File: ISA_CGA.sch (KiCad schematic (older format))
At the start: 29 parts, among them U1 74S112, U11 74LS74, U12 74LS393, U13 74LS08, U14 74LS32, U15 74LS00, U16 74LS04, U2 74LS74, U20 74LS04, U22 74LS51, U23 74LS32, U25 74LS00, U26 74LS04, U27 74LS51, U28 74LS10, U29 74S04, U3 74S86, U30 74LS32, U31 74S08, U41 74LS08, U42 74LS86, U46 74LS00, U47 74LS51, U48 74LS51, U49 74LS02, U6 74LS04, U62 74LS125, U65 74LS02, U68 74LS86

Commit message: More sheet 5
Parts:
- added U44: 74S74, Package_DIP:DIP-14_W7.62mm_LongPads, symbol 74xx:74LS74
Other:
- moved on the sheet: U29G, U30E, U31E, U41E, U42E
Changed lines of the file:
@@
 L 74xx:74LS08 U?
 U 5 1 61D13A76
-P 4150 5150
+P 3550 5150
 AR Path="/60463C10/61D13A76" Ref="U?"  Part="3"
 AR Path="/61D13A76" Ref="U31"  Part="5"
-F 0 "U31" H 4000 5500 50  0000 C CNN
-F 1 "74S08" H 4300 5500 50  0000 C CNN
-F 2 "Package_DIP:DIP-14_W7.62mm_LongPads" H 4150 5150 50  0001 C CNN
-F 3 "http://www.ti.com/lit/gpn/sn74LS08" H 4150 5150 50  0001 C CNN
-	5    4150 5150
+F 0 "U31" H 3400 5500 50  0000 C CNN
+F 1 "74S08" H 3700 5500 50  0000 C CNN
+F 2 "Package_DIP:DIP-14_W7.62mm_LongPads" H 3550 5150 50  0001 C CNN
+F 3 "http://www.ti.com/lit/gpn/sn74LS08" H 3550 5150 50  0001 C CNN
+	5    3550 5150
 	1    0    0    -1
 $EndComp
@@
 L 74xx:74LS86 U?
 U 5 1 629C2DFD
-P 5350 5150
+P 4750 5150
 AR Path="/60463C10/629C2DFD" Ref="U?"  Part="4"
 AR Path="/60463C57/629C2DFD" Ref="U?"  Part="1"
 AR Path="/629C2DFD" Ref="U42"  Part="5"
-F 0 "U42" H 5500 5500 50  0000 C CNN
-F 1 "74LS86" H 5200 5500 50  0000 C CNN
-F 2 "Package_DIP:DIP-14_W7.62mm_LongPads" H 5350 5150 50  0001 C CNN
-F 3 "74xx/74ls86.pdf" H 5350 5150 50  0001 C CNN
-	5    5350 5150
+F 0 "U42" H 4900 5500 50  0000 C CNN
+F 1 "74LS86" H 4600 5500 50  0000 C CNN
+F 2 "Package_DIP:DIP-14_W7.62mm_LongPads" H 4750 5150 50  0001 C CNN
+F 3 "74xx/74ls86.pdf" H 4750 5150 50  0001 C CNN
+	5    4750 5150
 	-1   0    0    -1
 $EndComp
@@
 L 74xx:74LS32 U?
 U 5 1 62AC6F3C
-P 3550 5150
+P 2950 5150
 AR Path="/60463C57/62AC6F3C" Ref="U?"  Part="3"
 AR Path="/62AC6F3C" Ref="U30"  Part="5"
-F 0 "U30" H 3400 5500 50  0000 C CNN
-F 1 "74LS32" H 3700 5500 50  0000 C CNN
-F 2 "" H 3550 5150 50  0001 C CNN
-F 3 "http://www.ti.com/lit/gpn/sn74LS32" H 3550 5150 50  0001 C CNN
-	5    3550 5150
+F 0 "U30" H 2800 5500 50  0000 C CNN
+F 1 "74LS32" H 3100 5500 50  0000 C CNN
+F 2 "" H 2950 5150 50  0001 C CNN
+F 3 "http://www.ti.com/lit/gpn/sn74LS32" H 2950 5150 50  0001 C CNN
+	5    2950 5150
 	1    0    0    -1
 $EndComp
@@
 L 74xx:74LS08 U?
 U 5 1 62CA5B30
-P 4750 5150
+P 4150 5150
 AR Path="/60463C57/62CA5B30" Ref="U?"  Part="4"
 AR Path="/62CA5B30" Ref="U41"  Part="5"
-F 0 "U41" H 4600 5500 50  0000 C CNN
-F 1 "74LS08" H 4900 5500 50  0000 C CNN
-F 2 "Package_DIP:DIP-14_W7.62mm_LongPads" H 4750 5150 50  0001 C CNN
-F 3 "http://www.ti.com/lit/gpn/sn74LS08" H 4750 5150 50  0001 C CNN
-	5    4750 5150
+F 0 "U41" H 4000 5500 50  0000 C CNN
+F 1 "74LS08" H 4300 5500 50  0000 C CNN
+F 2 "Package_DIP:DIP-14_W7.62mm_LongPads" H 4150 5150 50  0001 C CNN
+F 3 "http://www.ti.com/lit/gpn/sn74LS08" H 4150 5150 50  0001 C CNN
+	5    4150 5150
 	1    0    0    -1
 $EndComp
@@
 L 74xx:74LS04 U?
 U 7 1 63CE58E6
-P 2950 5150
+P 2350 5150
 AR Path="/60463C57/63CE58E6" Ref="U?"  Part="6"
 AR Path="/60463CC5/63CE58E6" Ref="U?"  Part="4"
 AR Path="/63CE58E6" Ref="U29"  Part="7"
-F 0 "U29" H 2800 5500 50  0000 C CNN
-F 1 "74S04" H 3100 5500 50  0000 C CNN
-F 2 "Package_DIP:DIP-14_W7.62mm_LongPads" H 2950 5150 50  0001 C CNN
-F 3 "http://www.ti.com/lit/gpn/sn74LS04" H 2950 5150 50  0001 C CNN
-	7    2950 5150
+F 0 "U29" H 2200 5500 50  0000 C CNN
+F 1 "74S04" H 2500 5500 50  0000 C CNN
+F 2 "Package_DIP:DIP-14_W7.62mm_LongPads" H 2350 5150 50  0001 C CNN
+F 3 "http://www.ti.com/lit/gpn/sn74LS04" H 2350 5150 50  0001 C CNN
+	7    2350 5150
 	1    0    0    -1
 $EndComp
@@
 	1    0    0    -1
 $EndComp
+$Comp
+L 74xx:74LS74 U?
+U 3 1 64BD6305
+P 5350 5150
+AR Path="/60463CF3/64BD6305" Ref="U?"  Part="1"
+AR Path="/64BD6305" Ref="U44"  Part="3"
+F 0 "U44" H 5200 5500 50  0000 C CNN
+F 1 "74S74" H 5500 5500 50  0000 C CNN
+F 2 "Package_DIP:DIP-14_W7.62mm_LongPads" H 5350 5150 50  0001 C CNN
+F 3 "74xx/74hc_hct74.pdf" H 5350 5150 50  0001 C CNN
+	3    5350 5150
+	1    0    0    -1
+$EndComp

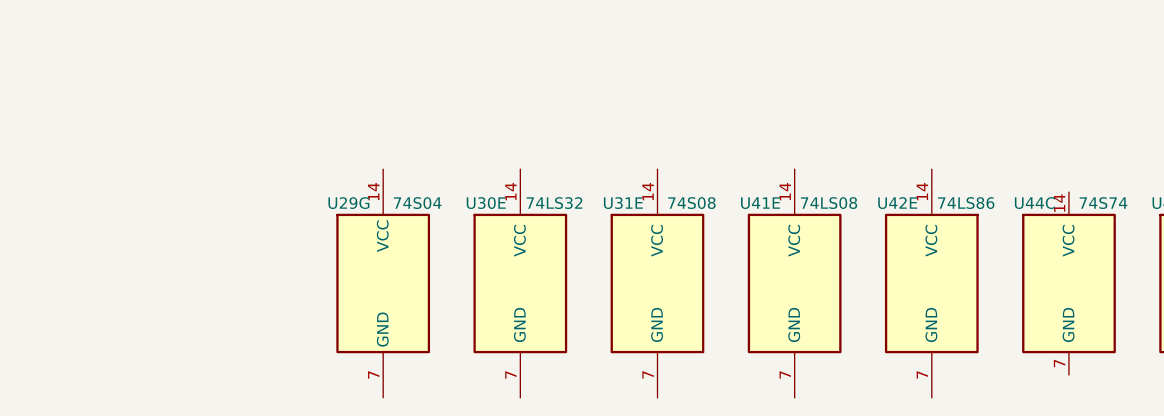
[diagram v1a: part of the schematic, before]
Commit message: More power connections for sheet 5
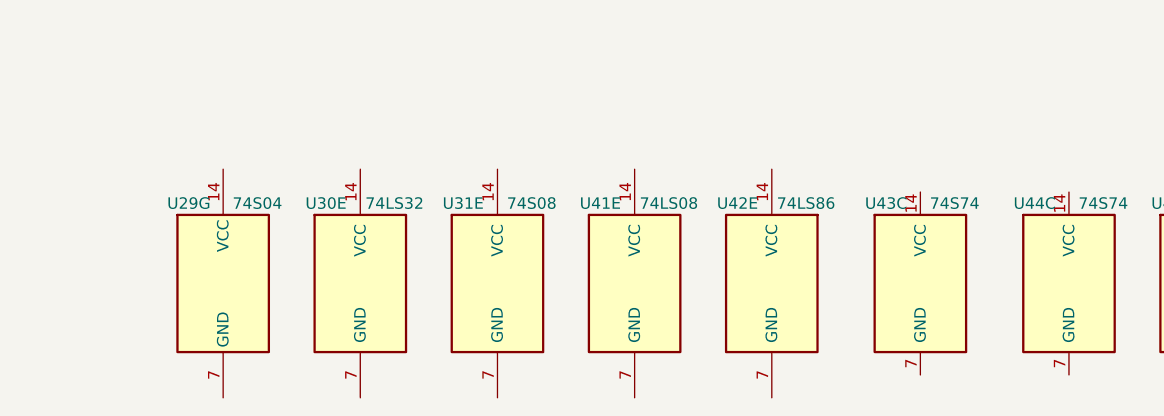
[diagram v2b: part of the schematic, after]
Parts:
- added U43: 74S74, Package_DIP:DIP-14_W7.62mm_LongPads, symbol 74xx:74LS74
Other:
- moved on the sheet: U29G, U30E, U31E, U41E, U42E
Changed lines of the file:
@@
 L 74xx:74LS08 U?
 U 5 1 61D13A76
-P 3550 5150
+P 2850 5150
 AR Path="/60463C10/61D13A76" Ref="U?"  Part="3"
 AR Path="/61D13A76" Ref="U31"  Part="5"
-F 0 "U31" H 3400 5500 50  0000 C CNN
-F 1 "74S08" H 3700 5500 50  0000 C CNN
-F 2 "Package_DIP:DIP-14_W7.62mm_LongPads" H 3550 5150 50  0001 C CNN
-F 3 "http://www.ti.com/lit/gpn/sn74LS08" H 3550 5150 50  0001 C CNN
-	5    3550 5150
+F 0 "U31" H 2700 5500 50  0000 C CNN
+F 1 "74S08" H 3000 5500 50  0000 C CNN
+F 2 "Package_DIP:DIP-14_W7.62mm_LongPads" H 2850 5150 50  0001 C CNN
+F 3 "http://www.ti.com/lit/gpn/sn74LS08" H 2850 5150 50  0001 C CNN
+	5    2850 5150
 	1    0    0    -1
 $EndComp
@@
 L 74xx:74LS86 U?
 U 5 1 629C2DFD
-P 4750 5150
+P 4050 5150
 AR Path="/60463C10/629C2DFD" Ref="U?"  Part="4"
 AR Path="/60463C57/629C2DFD" Ref="U?"  Part="1"
 AR Path="/629C2DFD" Ref="U42"  Part="5"
-F 0 "U42" H 4900 5500 50  0000 C CNN
-F 1 "74LS86" H 4600 5500 50  0000 C CNN
-F 2 "Package_DIP:DIP-14_W7.62mm_LongPads" H 4750 5150 50  0001 C CNN
-F 3 "74xx/74ls86.pdf" H 4750 5150 50  0001 C CNN
-	5    4750 5150
+F 0 "U42" H 4200 5500 50  0000 C CNN
+F 1 "74LS86" H 3900 5500 50  0000 C CNN
+F 2 "Package_DIP:DIP-14_W7.62mm_LongPads" H 4050 5150 50  0001 C CNN
+F 3 "74xx/74ls86.pdf" H 4050 5150 50  0001 C CNN
+	5    4050 5150
 	-1   0    0    -1
 $EndComp
@@
 L 74xx:74LS32 U?
 U 5 1 62AC6F3C
-P 2950 5150
+P 2250 5150
 AR Path="/60463C57/62AC6F3C" Ref="U?"  Part="3"
 AR Path="/62AC6F3C" Ref="U30"  Part="5"
-F 0 "U30" H 2800 5500 50  0000 C CNN
-F 1 "74LS32" H 3100 5500 50  0000 C CNN
-F 2 "" H 2950 5150 50  0001 C CNN
-F 3 "http://www.ti.com/lit/gpn/sn74LS32" H 2950 5150 50  0001 C CNN
-	5    2950 5150
+F 0 "U30" H 2100 5500 50  0000 C CNN
+F 1 "74LS32" H 2400 5500 50  0000 C CNN
+F 2 "" H 2250 5150 50  0001 C CNN
+F 3 "http://www.ti.com/lit/gpn/sn74LS32" H 2250 5150 50  0001 C CNN
+	5    2250 5150
 	1    0    0    -1
 $EndComp
@@
 L 74xx:74LS08 U?
 U 5 1 62CA5B30
-P 4150 5150
+P 3450 5150
 AR Path="/60463C57/62CA5B30" Ref="U?"  Part="4"
 AR Path="/62CA5B30" Ref="U41"  Part="5"
-F 0 "U41" H 4000 5500 50  0000 C CNN
-F 1 "74LS08" H 4300 5500 50  0000 C CNN
-F 2 "Package_DIP:DIP-14_W7.62mm_LongPads" H 4150 5150 50  0001 C CNN
-F 3 "http://www.ti.com/lit/gpn/sn74LS08" H 4150 5150 50  0001 C CNN
-	5    4150 5150
+F 0 "U41" H 3300 5500 50  0000 C CNN
+F 1 "74LS08" H 3600 5500 50  0000 C CNN
+F 2 "Package_DIP:DIP-14_W7.62mm_LongPads" H 3450 5150 50  0001 C CNN
+F 3 "http://www.ti.com/lit/gpn/sn74LS08" H 3450 5150 50  0001 C CNN
+	5    3450 5150
 	1    0    0    -1
 $EndComp
@@
 L 74xx:74LS04 U?
 U 7 1 63CE58E6
-P 2350 5150
+P 1650 5150
 AR Path="/60463C57/63CE58E6" Ref="U?"  Part="6"
 AR Path="/60463CC5/63CE58E6" Ref="U?"  Part="4"
 AR Path="/63CE58E6" Ref="U29"  Part="7"
-F 0 "U29" H 2200 5500 50  0000 C CNN
-F 1 "74S04" H 2500 5500 50  0000 C CNN
-F 2 "Package_DIP:DIP-14_W7.62mm_LongPads" H 2350 5150 50  0001 C CNN
-F 3 "http://www.ti.com/lit/gpn/sn74LS04" H 2350 5150 50  0001 C CNN
-	7    2350 5150
+F 0 "U29" H 1500 5500 50  0000 C CNN
+F 1 "74S04" H 1800 5500 50  0000 C CNN
+F 2 "Package_DIP:DIP-14_W7.62mm_LongPads" H 1650 5150 50  0001 C CNN
+F 3 "http://www.ti.com/lit/gpn/sn74LS04" H 1650 5150 50  0001 C CNN
+	7    1650 5150
 	1    0    0    -1
 $EndComp
@@
 	1    0    0    -1
 $EndComp
+$Comp
+L 74xx:74LS74 U?
+U 3 1 64C32517
+P 4700 5150
+AR Path="/60463CF3/64C32517" Ref="U?"  Part="1"
+AR Path="/64C32517" Ref="U43"  Part="3"
+F 0 "U43" H 4550 5500 50  0000 C CNN
+F 1 "74S74" H 4850 5500 50  0000 C CNN
+F 2 "Package_DIP:DIP-14_W7.62mm_LongPads" H 4700 5150 50  0001 C CNN
+F 3 "74xx/74hc_hct74.pdf" H 4700 5150 50  0001 C CNN
+	3    4700 5150
+	1    0    0    -1
+$EndComp

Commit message: Sheet 6
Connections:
- net VCC: now reaches U48.14 (VCC)
- net VCC: now also U1.16 (VCC), U11.14 (VCC), U12.14 (VCC), U13.14 (VCC), U14.14 (VCC), U15.14 (VCC), U16.14 (VCC), U2.14 (VCC), U20.14 (VCC), U22.14 (VCC), U23.14 (VCC), U25.14 (VCC), U26.14 (VCC), U27.14 (VCC), U28.14 (VCC), U29.14 (VCC), U3.14 (VCC), U30.14 (VCC), U31.14 (VCC), U41.14 (VCC), U42.14 (VCC), U46.14 (VCC), U47.14 (VCC), U49.14 (VCC), U6.14 (VCC), U62.14 (VCC), U65.14 (VCC), U68.14 (VCC)
- net GND: now reaches U48.7 (GND)
- net GND: now also U1.8 (GND), U11.7 (GND), U12.7 (GND), U13.7 (GND), U14.7 (GND), U15.7 (GND), U16.7 (GND), U2.7 (GND), U20.7 (GND), U22.7 (GND), U23.7 (GND), U25.7 (GND), U26.7 (GND), U27.7 (GND), U28.7 (GND), U29.7 (GND), U3.7 (GND), U30.7 (GND), U31.7 (GND), U41.7 (GND), U42.7 (GND), U46.7 (GND), U47.7 (GND), U49.7 (GND), U6.7 (GND), U62.7 (GND), U65.7 (GND), U68.7 (GND)
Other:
- moved on the sheet: U29G, U30E, U31E, U41E, U42E, U43C, U44C, U46E, U47C, U48C, U49E, U62E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

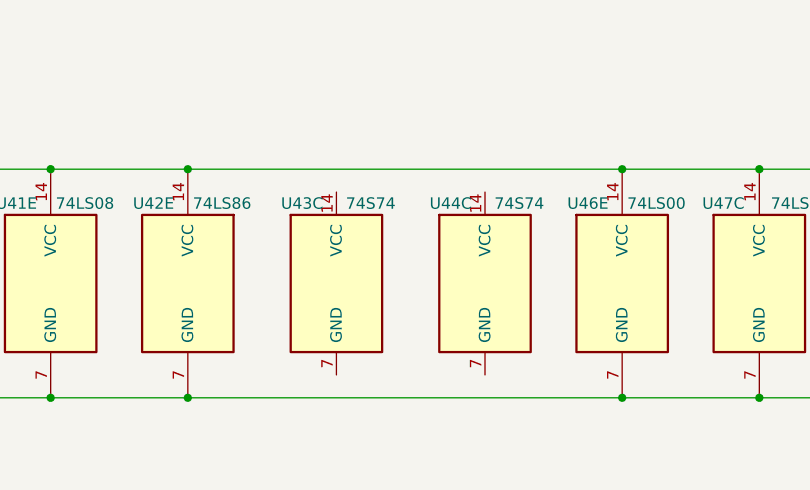
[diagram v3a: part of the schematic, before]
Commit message: Add missing connection to Vcc/GND for two ICs
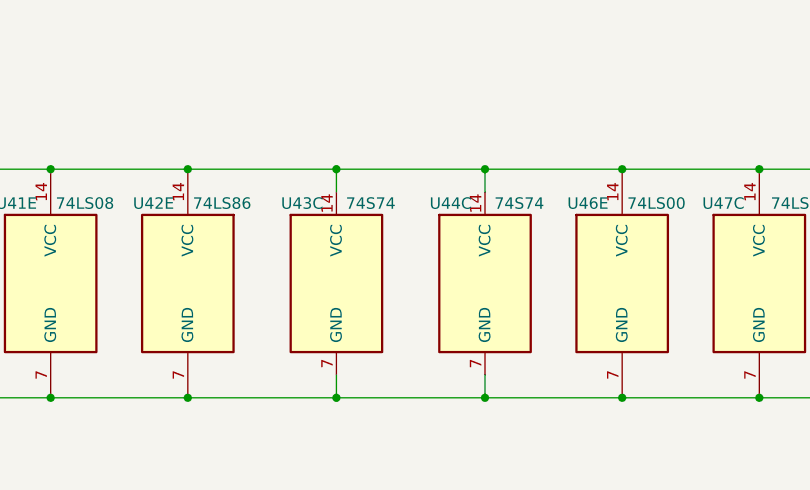
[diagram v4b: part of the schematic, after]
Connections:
- net GND: now also U43.7 (GND), U44.7 (GND)
- net VCC: now also U43.14 (VCC), U44.14 (VCC)
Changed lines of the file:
@@
 Connection ~ 5200 4700
 Wire Wire Line
-	5200 4700 3300 4700
+	5200 4700 4600 4700
 Connection ~ 5800 4700
 Wire Wire Line
@@
 Connection ~ 3300 5700
 Wire Wire Line
-	3300 5700 5200 5700
+	3300 5700 3950 5700
 Connection ~ 5200 5700
 Wire Wire Line
@@
 Wire Wire Line
 	3300 3850 2700 3850
+Wire Wire Line
+	3950 4800 3950 4700
+Connection ~ 3950 4700
+Wire Wire Line
+	3950 4700 3300 4700
+Wire Wire Line
+	4600 4800 4600 4700
+Connection ~ 4600 4700
+Wire Wire Line
+	4600 4700 3950 4700
+Wire Wire Line
+	4600 5600 4600 5700
+Connection ~ 4600 5700
+Wire Wire Line
+	4600 5700 5200 5700
+Wire Wire Line
+	3950 5600 3950 5700
+Connection ~ 3950 5700
+Wire Wire Line
+	3950 5700 4600 5700
 $EndSCHEMATC

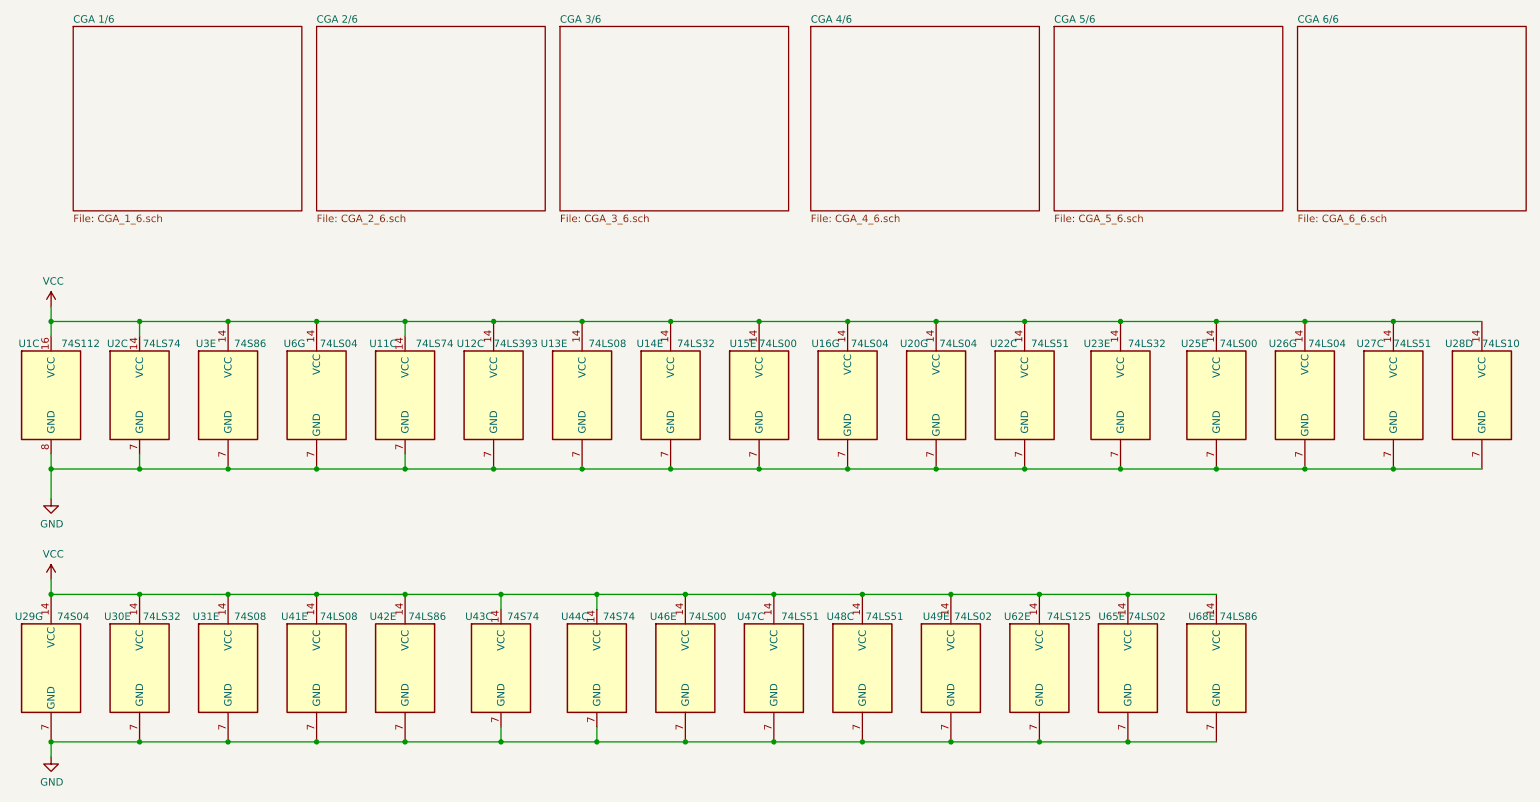
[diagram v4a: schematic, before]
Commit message: Fixed some duplicate units and mislabeling
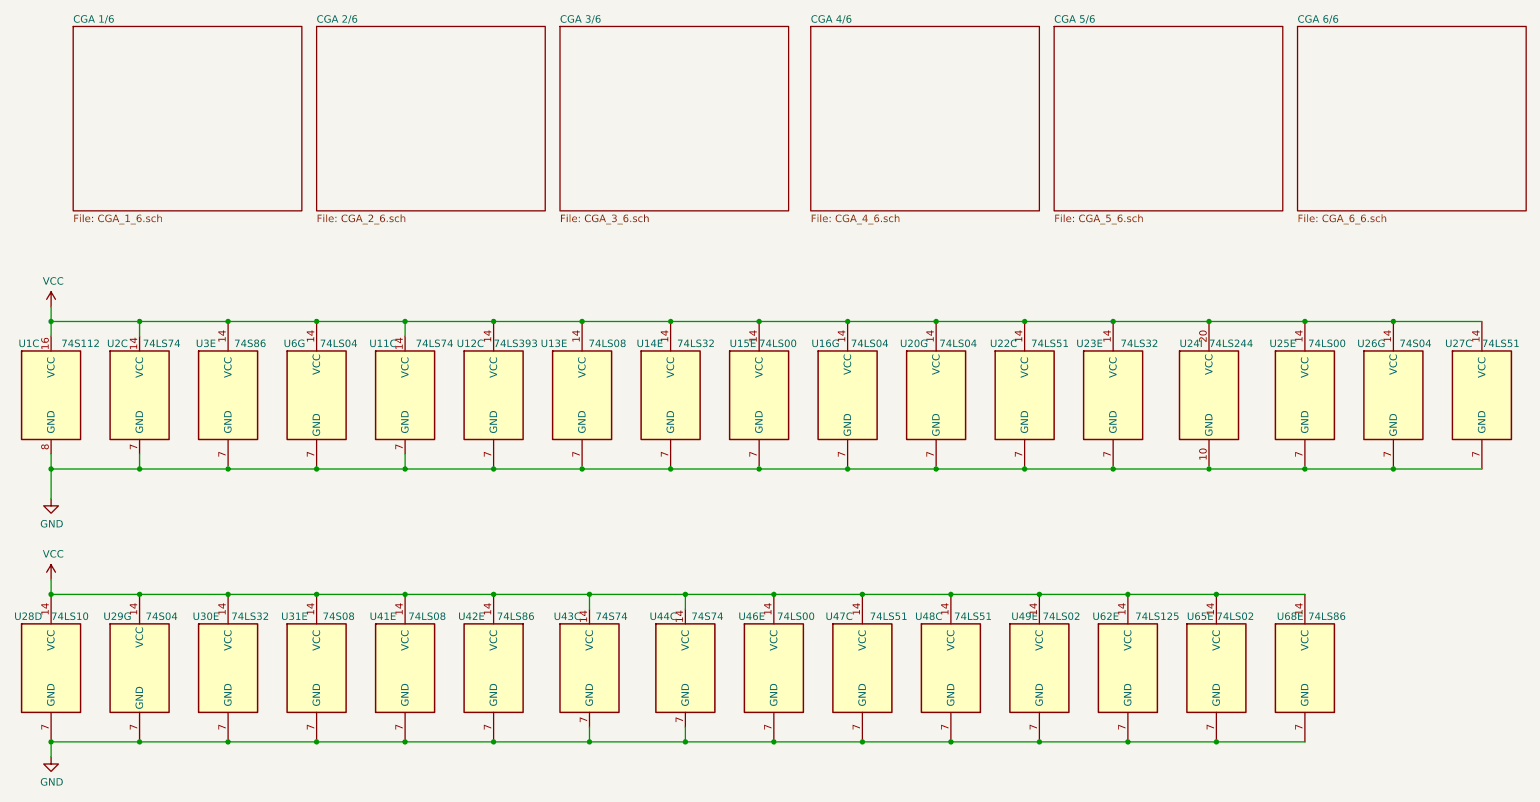
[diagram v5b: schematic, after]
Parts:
- added U24: 74LS244, Package_DIP:DIP-20_W7.62mm_LongPads, symbol 74xx:74LS244_Split
- U26: value 74LS04 -> 74S04
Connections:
- net GND: now also U24.10 (GND)
- net VCC: now also U24.20 (VCC)
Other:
- moved on the sheet: U23E, U25E, U26G, U27C, U28D, U29G, U30E, U31E, U41E, U42E, U43C, U44C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

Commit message: Fix some more flags and footprints
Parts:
- U62: footprint Package_DIP:DIP-14_W10.16mm_LongPads -> Package_DIP:DIP-14_W7.62mm_LongPads

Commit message: Laying out more components
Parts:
- U30: footprint (none) -> Package_DIP:DIP-14_W7.62mm_LongPads
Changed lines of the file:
@@
 F 0 "U30" H 1950 5550 50  0000 C CNN
 F 1 "74LS32" H 2250 5550 50  0000 C CNN
-F 2 "" H 2100 5200 50  0001 C CNN
+F 2 "Package_DIP:DIP-14_W7.62mm_LongPads" H 2100 5200 50  0001 C CNN
 F 3 "http://www.ti.com/lit/gpn/sn74LS32" H 2100 5200 50  0001 C CNN
 	5    2100 5200

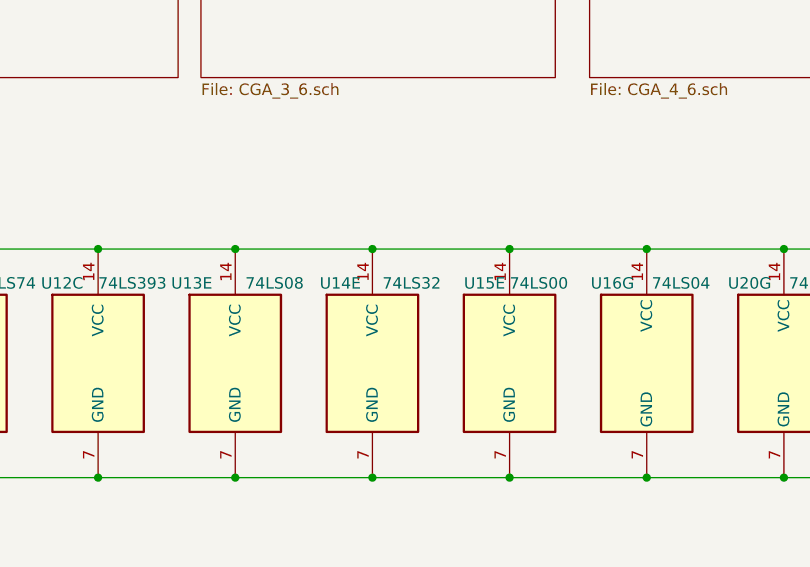
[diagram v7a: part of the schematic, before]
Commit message: Reorganize space between ICs
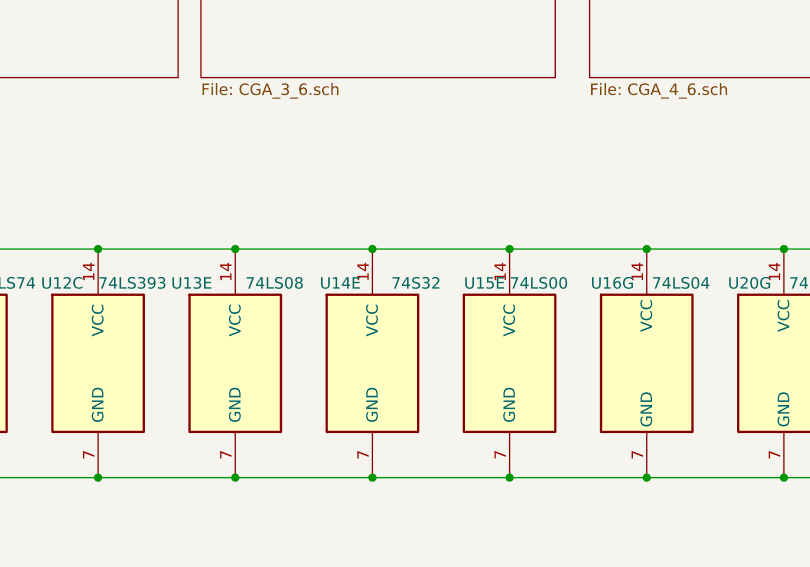
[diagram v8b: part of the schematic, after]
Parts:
- U14: value 74LS32 -> 74S32
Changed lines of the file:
@@
 AR Path="/607513C2" Ref="U14"  Part="5"
 F 0 "U14" H 5050 3700 50  0000 R CNN
-F 1 "74LS32" H 5400 3700 50  0000 R CNN
+F 1 "74S32" H 5400 3700 50  0000 R CNN
 F 2 "Package_DIP:DIP-14_W7.62mm_LongPads" H 5100 3350 50  0001 C CNN
 F 3 "http://www.ti.com/lit/gpn/sn74LS32" H 5100 3350 50  0001 C CNN
